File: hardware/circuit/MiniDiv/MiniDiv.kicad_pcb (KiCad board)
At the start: 2 copper layers, 65 x 128.5 mm, 85 parts, among them J1 Conn_01x10_Pin, SW1 SW_DPDT_x2, U1 40106, U2 LM358, U3 40106, U4 LM317_SOT-223, U5 CD4040

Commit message: Updated PCBs
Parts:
- C2, C3: footprint Capacitor_SMD:CP_Elec_6.3x4.5 -> Capacitor_SMD:CP_Elec_4x3.9; moved to B.Cu
- U2: footprint Package_SO:SOIC-8_3.9x4.9mm_P1.27mm -> Package_SO:SOIC-8_5.23x5.23mm_P1.27mm
- U5: footprint Package_SO:SOIC-16_3.9x9.9mm_P1.27mm -> Package_SO:SOIC-16W_5.3x10.2mm_P1.27mm
- moved R2 1.31 mm to (95.1, 57.5)
- moved C3 1.10 mm to (106.6, 102.0)
- moved R4 1.05 mm to (99.5, 57.9)
- moved C2 1.00 mm to (106.6, 94.0)
- moved R3 0.75 mm to (112.3, 63.1)
- moved C6 0.65 mm to (117.8, 63.9)
- moved U5 0.17 mm to (114.3, 69.6)
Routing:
- net VREF: track 43.7 -> 48.0 mm
- net Net-(U5-Q1): track 29.8 -> 25.7 mm
- net Net-(U5-Q7): track 50.4 -> 47.4 mm
- net Net-(U5-Q2): track 30.1 -> 32.5 mm
- net Net-(U5-Q3): track 33.6 -> 35.9 mm
- net /RESET: track 17.0 -> 18.7 mm
- net /CLOCK: track 19.1 -> 20.6 mm
- net Net-(U5-Q6): track 46.8 -> 45.3 mm
- net Net-(U5-Q5): track 45.5 -> 46.7 mm
- net +12V: track 66.2 -> 67.4 mm
- net +10V: track 104.9 -> 104.0 mm
- net Net-(D2-K): track 12.0 -> 11.1 mm
- net -12V: track 10.6 -> 9.82 mm
- net Net-(D4-A): track 6.12 -> 5.38 mm
- net Net-(D1-K): track 7.90 -> 8.63 mm
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
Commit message: Added drawings and photos
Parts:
- U5: value CD4040 -> CD4040BNSR

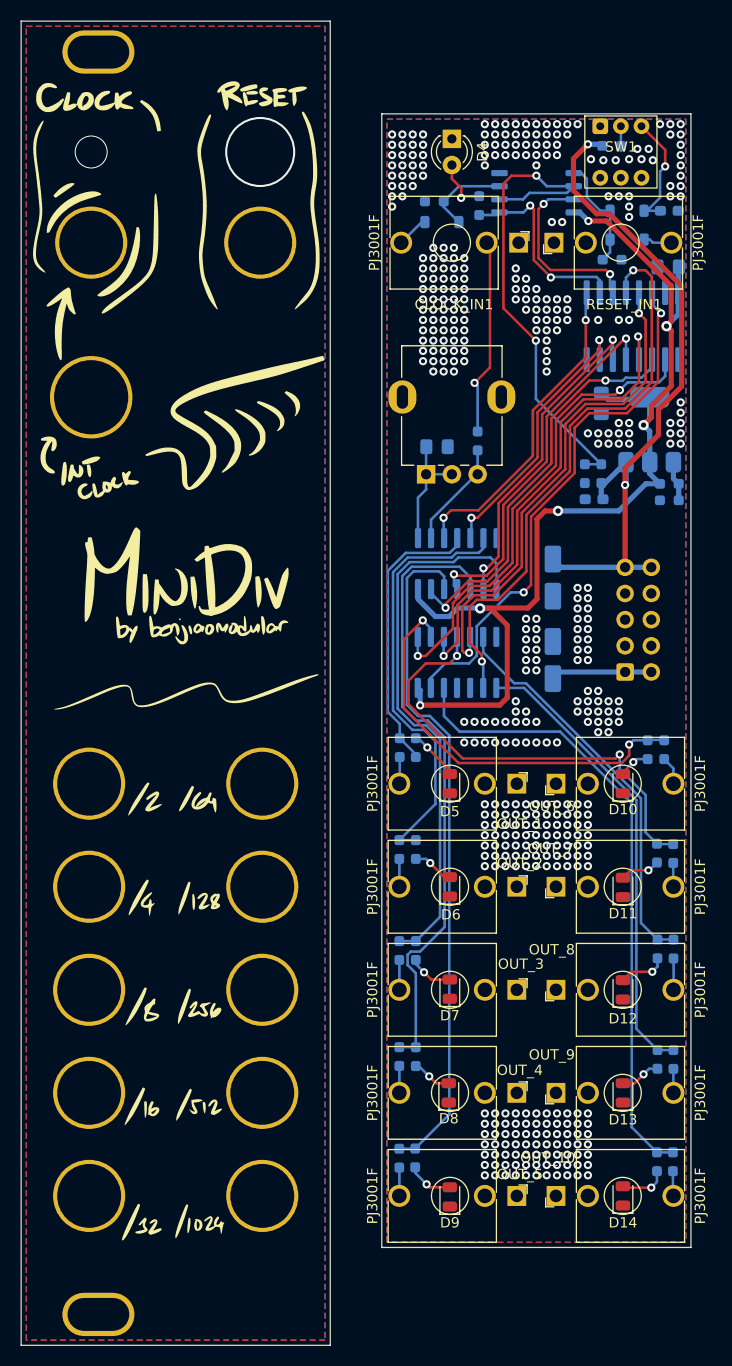
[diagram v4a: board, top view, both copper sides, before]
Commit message: Fixed LED clearance issues
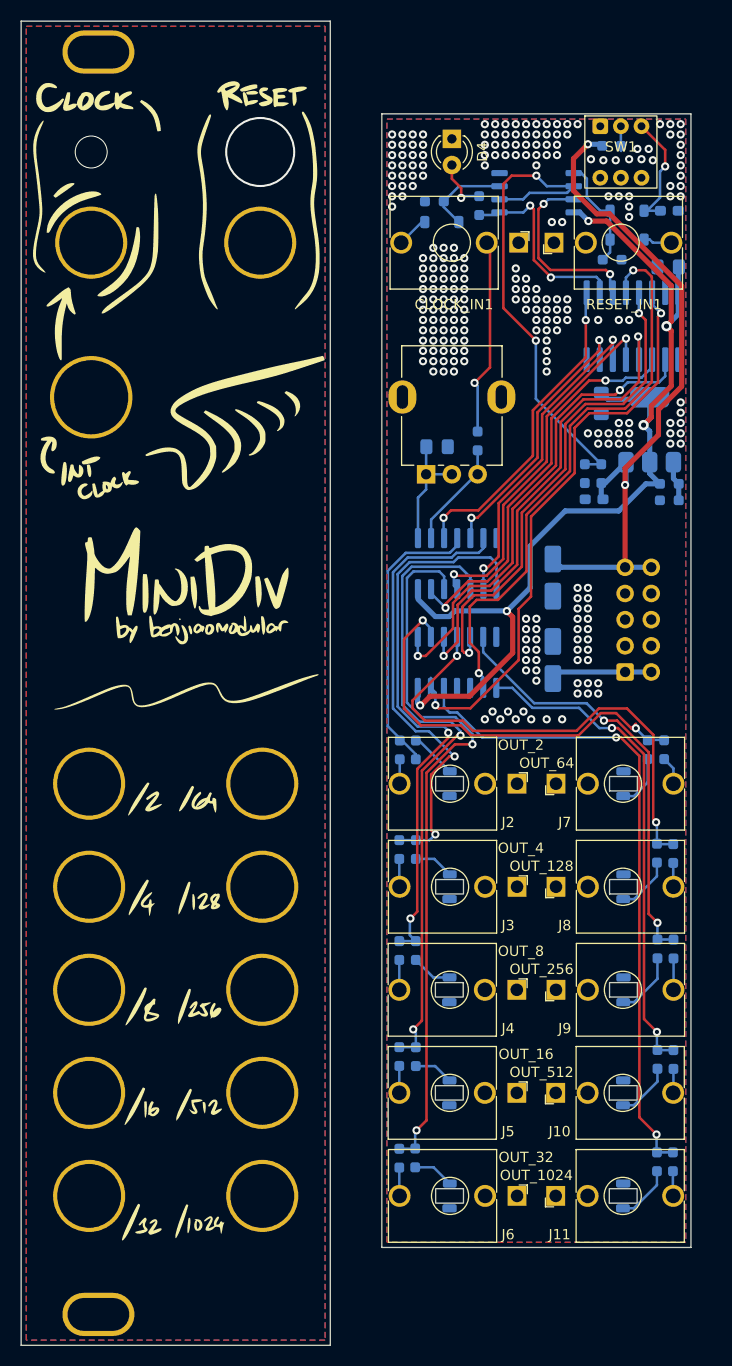
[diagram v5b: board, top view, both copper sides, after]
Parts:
- removed D10, D11, D12, D13, D14, D5, D6, D7, D8, D9: LED, LED_SMD:LED_0805_2012Metric
- removed OUT_1, OUT_10, OUT_2, OUT_3, OUT_4, OUT_5, OUT_6, OUT_7, OUT_8, OUT_9: PJ3001F, benjiaomodular:AudioJack_3.5mm
- added J10: OUT_512, benjiaomodular:AudioJack_PJ3001F_0805LED, F.Cu at (106.9, 144.0)
- added J11: OUT_1024, benjiaomodular:AudioJack_PJ3001F_0805LED, F.Cu at (106.9, 154.0)
- added J2: OUT_2, benjiaomodular:AudioJack_PJ3001F_0805LED, F.Cu at (103.1, 114.0)
- added J3: OUT_4, benjiaomodular:AudioJack_PJ3001F_0805LED, F.Cu at (103.1, 124.0)
- added J4: OUT_8, benjiaomodular:AudioJack_PJ3001F_0805LED, F.Cu at (103.1, 134.0)
- added J5: OUT_16, benjiaomodular:AudioJack_PJ3001F_0805LED, F.Cu at (103.1, 144.0)
- added J6: OUT_32, benjiaomodular:AudioJack_PJ3001F_0805LED, F.Cu at (103.1, 154.0)
- added J7: OUT_64, benjiaomodular:AudioJack_PJ3001F_0805LED, F.Cu at (106.9, 114.0)
- added J8: OUT_128, benjiaomodular:AudioJack_PJ3001F_0805LED, F.Cu at (106.9, 124.0)
- added J9: OUT_256, benjiaomodular:AudioJack_PJ3001F_0805LED, F.Cu at (106.9, 134.0)
- moved R10 0.22 mm to (93.3, 110.7)
- moved R14 0.22 mm to (91.7, 110.7)
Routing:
- net +10V: track 104.0 -> 98.1 mm, vias 6 -> 5
- net Net-(U5-Q9): track 51.6 -> 56.3 mm
- net /OUT_32: track 66.0 -> 70.1 mm, vias 0 -> 2
- net /OUT_512: track 44.7 -> 47.8 mm, vias 0 -> 2
- net /OUT_256: track 38.6 -> 41.7 mm, vias 0 -> 2
- net /OUT_128: track 44.4 -> 47.3 mm
- net /OUT_1024: track 60.9 -> 63.5 mm, vias 0 -> 2
- net /OUT_4: track 42.1 -> 44.6 mm, vias 0 -> 2
- net Net-(J7-Pad2): track 3.09 -> 5.19 mm, vias 1 -> 0
- net /OUT_8: track 53.5 -> 55.5 mm, vias 0 -> 2
- net /OUT_16: track 60.6 -> 62.2 mm, vias 0 -> 2
- net Net-(J8-Pad2): track 3.91 -> 5.52 mm, vias 1 -> 0
- net Net-(J10-Pad2): track 3.93 -> 5.54 mm, vias 1 -> 0
- net Net-(J9-Pad2): track 4.70 -> 6.25 mm, vias 1 -> 0
- net Net-(J11-Pad2): track 4.63 -> 5.58 mm, vias 1 -> 0
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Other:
- board text added: "MiniDiv v0.3"
- board text removed: "MiniDiv v0.2"
